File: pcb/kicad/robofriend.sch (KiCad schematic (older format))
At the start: 139 parts, among them J1 BAT1, J10 US3, J11 US4, J12 I2C, J13 I2C, J14 I2C, J15 I2C, J16 12VOUT, J17 5VIN, J18 5VOUT, J19 5VOUT, J2 BAT2, J20 USB_A_4_PIN, J21 MON/AMP, J22 ADC4, J23 MRi, J24 SPI, J25 ADC4, J26 MLe, J27 M1, J28 M2, J29 ADC1, J3 BAT3, J30 ADC2, J31 UART, J32 ADC3, J33 GS2, J4 PWR, J5 US1, J6 3V3OUT, J7 3V3OUT, J8 GS2, J9 US2, K1 SCHRACK-RTx3, Q1 NMOS, Q2 NMOS, Q3 NMOS, Q4 NPN, Q5 PMOS, Q6 NMOS, Q7 NMOS, U1 LM3940-3.3, U2 Teensy++2.0, U3 TL331, U4 LM4040, U5 MCP6001, U6 INA193, U7 TL331

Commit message: first steps of layouting done
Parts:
- C11: footprint Capacitors_SMD:CP_Elec_6.3x5.3 -> Capacitors_SMD:CP_Elec_6.3x5.8; Part No (none) -> EEEFK1C470P
- C12: footprint Capacitors_SMD:CP_Elec_10x10 -> Capacitors_SMD:CP_Elec_8x10.5; Part No (none) -> EEEFK1C471P
- C4: footprint Capacitors_SMD:CP_Elec_4x5.8 -> Capacitors_SMD:CP_Elec_4x5.7; Part No (none) -> EEE0JA330WR
- C5: value 0.1u -> 100u; footprint (none) -> Capacitors_SMD:CP_Elec_6.3x5.7; Part No (none) -> EEE1CA101WAP
- C6: footprint (none) -> Capacitors_SMD:CP_Elec_5x5.7; Part No (none) -> EEE1CA330WR
- D15, D16: footprint Diodes_SMD:D_SOD-123 -> Diodes_SMD:D_SOD-323
- D2: footprint Diodes_SMD:D_SOD-523 -> Diodes_SMD:D_SOD-323
- J20: Part No (none) -> 48258-0001
- R22: Part No (none) -> ERJ-M1WSJ10MU
- RV1, RV2: Part No (none) -> 3296W-1-104LF
- U3: footprint (none) -> TO_SOT_Packages_SMD:SOT-23-5
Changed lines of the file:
@@
 F 2 "Resistors_SMD:R_2512" V 12430 2250 50  0001 C CNN
 F 3 "" H 12500 2250 50  0001 C CNN
+F 4 "ERJ-M1WSJ10MU" V 12500 2250 60  0001 C CNN "Part No"
 	1    12500 2250
 	1    0    0    -1
@@
 F 2 "Potentiometers:Potentiometer_Trimmer_Bourns_3296W" H 14450 2750 50  0001 C CNN
 F 3 "" H 14450 2750 50  0001 C CNN
+F 4 "3296W-1-104LF" V 14450 2750 60  0001 C CNN "Part No"
 	1    14450 2750
 	1    0    0    -1
@@
 F 0 "C4" H 2025 4950 50  0000 L CNN
 F 1 "33u" H 2025 4750 50  0000 L CNN
-F 2 "Capacitors_SMD:CP_Elec_4x5.8" H 2038 4700 50  0001 C CNN
+F 2 "Capacitors_SMD:CP_Elec_4x5.7" H 2038 4700 50  0001 C CNN
 F 3 "" H 2000 4850 50  0001 C CNN
+F 4 "EEE0JA330WR" H 2000 4850 60  0001 C CNN "Part No"
 	1    2000 4850
 	1    0    0    -1
@@
 F 0 "C11" H 5770 4940 50  0000 L CNN
 F 1 "47u" H 5775 4750 50  0000 L CNN
-F 2 "Capacitors_SMD:CP_Elec_6.3x5.3" H 5788 4700 50  0001 C CNN
+F 2 "Capacitors_SMD:CP_Elec_6.3x5.8" H 5788 4700 50  0001 C CNN
 F 3 "" H 5750 4850 50  0001 C CNN
+F 4 "EEEFK1C470P" H 5750 4850 60  0001 C CNN "Part No"
 	1    5750 4850
 	1    0    0    -1
@@
 F 0 "C12" H 6270 4940 50  0000 L CNN
 F 1 "470u" H 6275 4750 50  0000 L CNN
-F 2 "Capacitors_SMD:CP_Elec_10x10" H 6288 4700 50  0001 C CNN
+F 2 "Capacitors_SMD:CP_Elec_8x10.5" H 6288 4700 50  0001 C CNN
 F 3 "" H 6250 4850 50  0001 C CNN
+F 4 "EEEFK1C471P" H 6250 4850 60  0001 C CNN "Part No"
 	1    6250 4850
 	1    0    0    -1
@@
 F 2 "USB_A_4_PIN:MOLEX_48258_0001" H 7675 1625 50  0001 C CNN
 F 3 "" H 7675 1625 50  0001 C CNN
+F 4 "48258-0001" H 7525 1675 60  0001 C CNN "Part No"
 	1    7525 1675
 	1    0    0    -1
@@
 F 0 "D15" H 11150 4600 50  0000 C CNN
 F 1 "BAT54" H 11150 4400 50  0000 C CNN
-F 2 "Diodes_SMD:D_SOD-123" H 11150 4500 50  0001 C CNN
+F 2 "Diodes_SMD:D_SOD-323" H 11150 4500 50  0001 C CNN
 F 3 "" H 11150 4500 50  0001 C CNN
 	1    11150 4500
@@
 F 0 "D16" H 11150 5100 50  0000 C CNN
 F 1 "BAT54" H 11150 4900 50  0000 C CNN
-F 2 "Diodes_SMD:D_SOD-123" H 11150 5000 50  0001 C CNN
+F 2 "Diodes_SMD:D_SOD-323" H 11150 5000 50  0001 C CNN
 F 3 "" H 11150 5000 50  0001 C CNN
 	1    11150 5000
@@
 F 0 "C6" H 3575 3250 50  0000 L CNN
 F 1 "33u" H 3575 3050 50  0000 L CNN
-F 2 "" H 3588 3000 50  0001 C CNN
+F 2 "Capacitors_SMD:CP_Elec_5x5.7" H 3588 3000 50  0001 C CNN
 F 3 "" H 3550 3150 50  0001 C CNN
+F 4 "EEE1CA330WR" H 3550 3150 60  0001 C CNN "Part No"
 	1    3550 3150
 	1    0    0    -1
@@
 F 2 "Potentiometers:Potentiometer_Trimmer_Bourns_3296W" H 2700 2350 50  0001 C CNN
 F 3 "" H 2700 2350 50  0001 C CNN
+F 4 "3296W-1-104LF" V 2700 2350 60  0001 C CNN "Part No"
 	1    2700 2350
 	1    0    0    -1
@@
 F 0 "D2" H 3450 1750 50  0000 C CNN
 F 1 "D" H 3450 1550 50  0000 C CNN
-F 2 "Diodes_SMD:D_SOD-523" H 3450 1650 50  0001 C CNN
+F 2 "Diodes_SMD:D_SOD-323" H 3450 1650 50  0001 C CNN
 F 3 "" H 3450 1650 50  0001 C CNN
 	1    3450 1650
@@
 F 0 "U3" H 3550 2450 50  0000 L CNN
 F 1 "TL331" H 3550 2050 50  0000 L CNN
-F 2 "" H 3550 2250 50  0001 L CNN
+F 2 "TO_SOT_Packages_SMD:SOT-23-5" H 3550 2250 50  0001 L CNN
 F 3 "" H 3550 2250 50  0001 C CNN
 	1    3550 2250
@@
 P 2700 1650
 F 0 "C5" H 2725 1750 50  0000 L CNN
-F 1 "0.1u" H 2725 1550 50  0000 L CNN
-F 2 "" H 2738 1500 50  0001 C CNN
+F 1 "100u" H 2725 1550 50  0000 L CNN
+F 2 "Capacitors_SMD:CP_Elec_6.3x5.7" H 2738 1500 50  0001 C CNN
 F 3 "" H 2700 1650 50  0001 C CNN
+F 4 "EEE1CA101WAP" H 2700 1650 60  0001 C CNN "Part No"
 	1    2700 1650
 	1    0    0    -1

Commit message: added plugs for buck-boost converter module
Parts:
- removed C23, C25: 100n, Capacitors_SMD:C_0603, symbol C
- removed D10: D, Diodes_SMD:D_SOD-523, symbol D
- removed D5: D, Diodes_SMD:D_SMC, symbol D
- removed D6: D, Diodes_SMD:D_SMB, symbol D
- removed D7: D, Diodes_SMD:D_SMA, symbol D
- removed D8: D, Diodes_SMD:D_SOD-123, symbol D
- removed D9: D, Diodes_SMD:D_SOD-323, symbol D
- removed J1: BAT1, Connectors_Molex:Molex_MiniFit-JR-5556-02B_2x01x4.20mm_Straight, symbol Screw_Terminal_01x02
- removed J2: BAT2, Connectors_Molex:Molex_MiniFit-JR-5556-02B_2x01x4.20mm_Straight, symbol Screw_Terminal_01x02
- removed J3: BAT3, Connectors_Molex:Molex_MiniFit-JR-5556-02B_2x01x4.20mm_Straight, symbol Screw_Terminal_01x02
- added C? (x2): 100n, Capacitors_SMD:C_0603, symbol C
- added J1: PWR, Connectors_Molex:Molex_MiniFit-JR-5556-06A_2x03x4.20mm_Straight, symbol Conn_02x03_Top_Bottom
- added J?: UART, Pin_Headers:Pin_Header_Straight_1x04_Pitch2.54mm, symbol Conn_01x04
- added J?: 12V-Buck-Boost, Connectors_Molex:Molex_MiniFit-JR-5556-02B_2x01x4.20mm_Straight, symbol Screw_Terminal_01x02
- added J?: 12V-Reg, Connectors_Molex:Molex_MiniFit-JR-5556-02B_2x01x4.20mm_Straight, symbol Screw_Terminal_01x02
- added U8: TXS0102, Housings_SSOP:SSOP-8_2.95x2.8mm_Pitch0.65mm, symbol TXB0102DCT
- D15, D16: Part No (none) -> BAT54WS-7-F
- D20: value BAT54 -> DB2X41500L; Part No (none) -> DB2X41500L
- J16: value 12VOUT -> 12V-Buck
- J22: value ADC4 -> ADC1
- J25: value ADC4 -> ADC2
- J29: value ADC1 -> IR1
- J30: value ADC2 -> IR2
- J32: value ADC3 -> IR3
- Q5: footprint TO_SOT_Packages_THT:TO-220-3_Vertical -> TO_SOT_Packages_SMD:TO-263-2; Part No (none) -> IRF4905STRLPBF
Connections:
- net +12V: now also J?.1 (Pin_1); no longer J21.1 (Pin_1), J21.2 (Pin_2)
- net +3V3: now also C?.1, J?.1 (Pin_1), U8.3 (VCCA), U8.6 (OE)
- net +5V: now also C?.1, U8.7 (VCCB)
- net +SW: now also K1.14, J1.1 (Pin_1), J1.2 (Pin_2), J1.3 (Pin_3)
- net -SW: now also J4.3 (Pin_3); no longer J4.6 (Pin_6), K1.14
- net D2: now also U8.8 (B1)
- net D3: now also U8.1 (B2)
- net GND: now also J4.6 (Pin_6), C?.2, C?.2, J1.4 (Pin_4), J1.5 (Pin_5), J1.6 (Pin_6), J?.2 (Pin_2), J?.2 (Pin_2), J?.4 (Pin_4), U8.2 (GND); no longer J4.3 (Pin_3)
- new net: J21.1 (Pin_1), J21.2 (Pin_2), J?.1 (Pin_1)
- new net: J?.3 (Pin_3), U8.4 (A2)
- new net: J?.2 (Pin_2), U8.5 (A1)
- no-connect marks 32 -> 20
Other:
- moved on the sheet: J17, J18, J19, J20, J21, J31, JP6, Q6, Q7, R27, R28, R30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

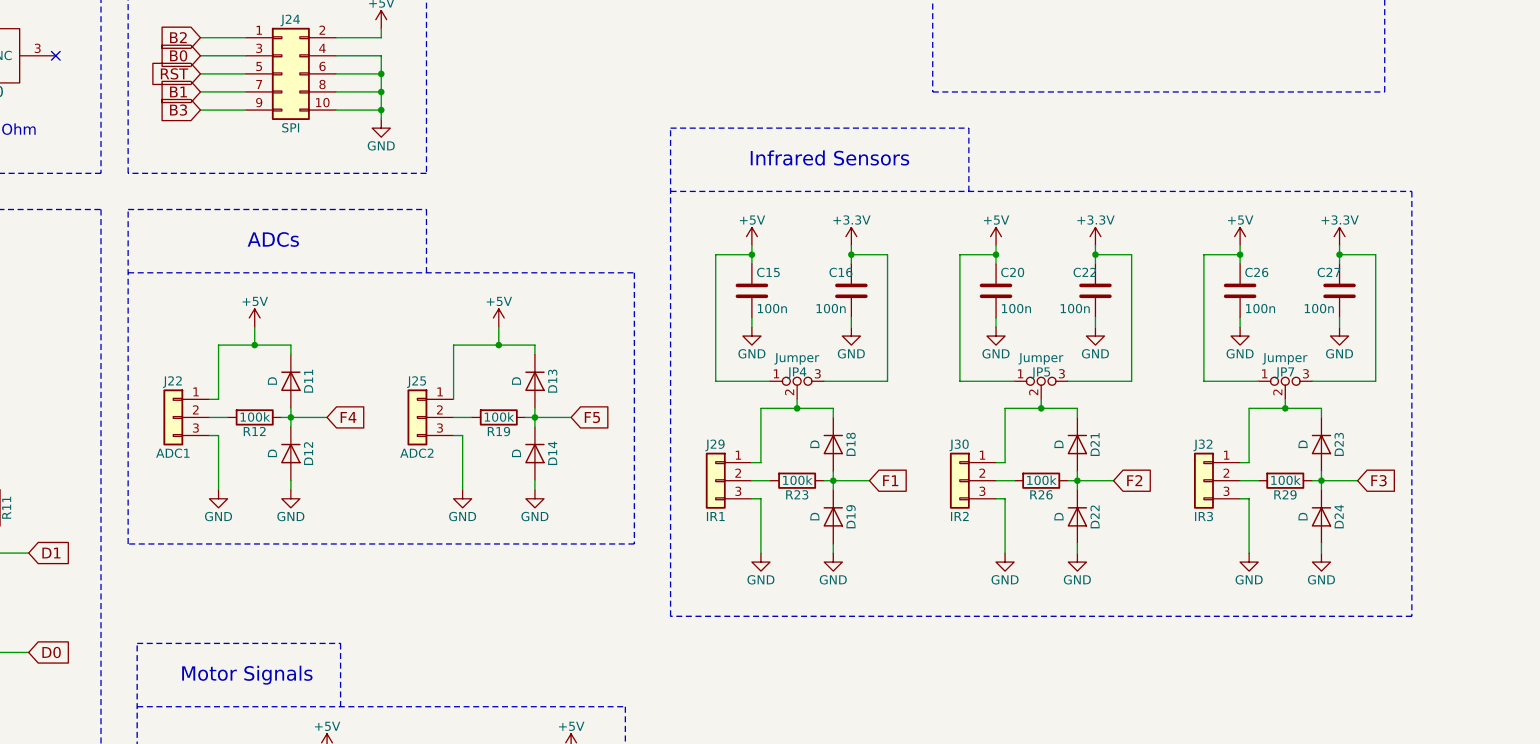
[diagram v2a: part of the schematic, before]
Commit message: removed extra jumpers and 100n capacitors for infrared sensors
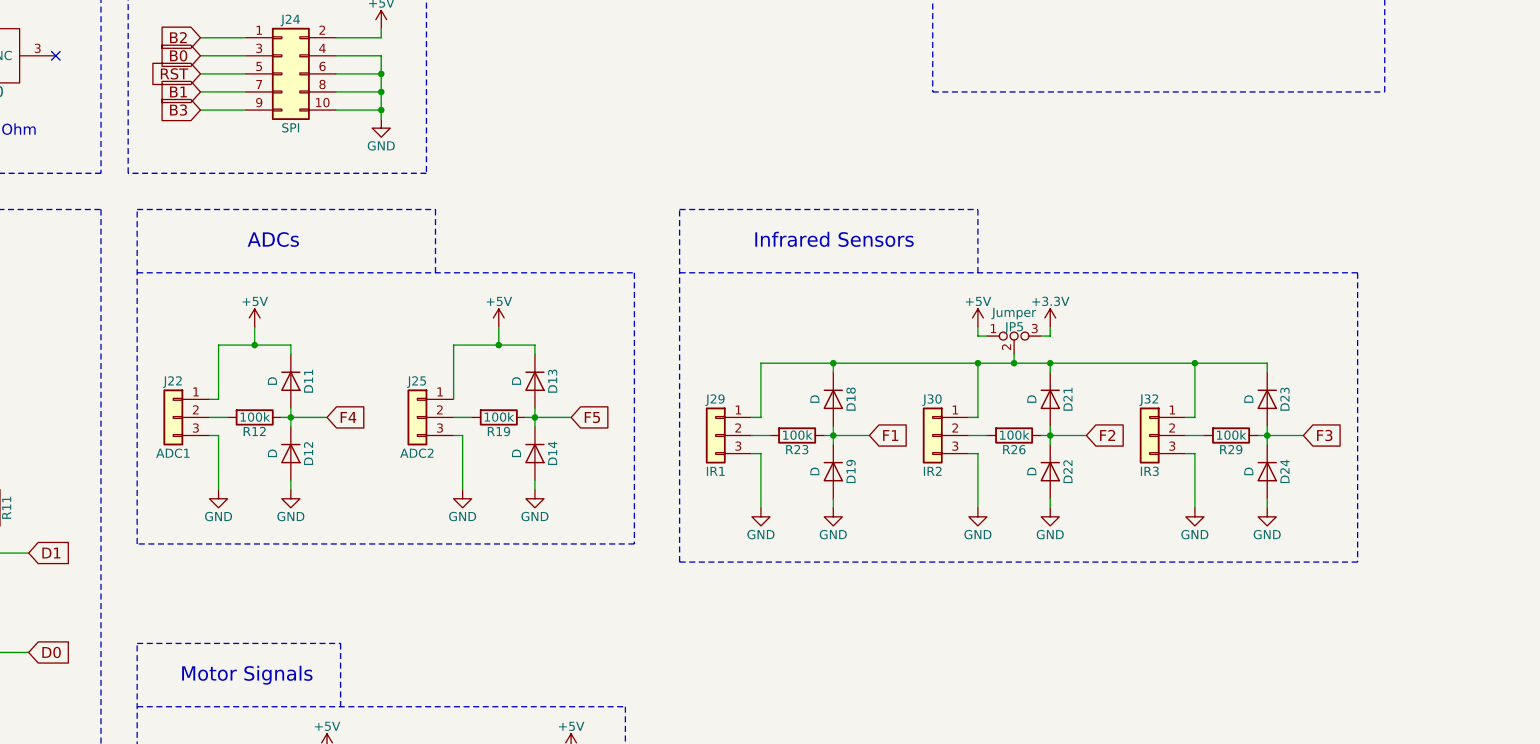
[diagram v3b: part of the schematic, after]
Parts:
- removed C15, C16, C20, C22, C26, C27: 100n, Capacitors_SMD:C_0603, symbol C
- removed JP4, JP7: Jumper, Pin_Headers:Pin_Header_Straight_1x03_Pitch2.54mm, symbol Jumper_NC_Dual
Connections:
- net at D21.1 (K), J30.1 (Pin_1), JP5.2: now also D18.1 (K), D23.1 (K), J29.1 (Pin_1), J32.1 (Pin_1)
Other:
- moved on the sheet: D18, D19, D21, D22, D23, D24, J29, J30, J32, JP5, R23, R26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
